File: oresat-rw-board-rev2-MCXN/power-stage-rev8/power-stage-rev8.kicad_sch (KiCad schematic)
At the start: 107 parts, among them IC1 MCXN947VDFT, J1 SM14B-SHLS-TF, J2 MEZZ, J3 Motor, U1 TCAN330, U2 MA732, U3 TPSM82901, U4 TPSM828214, U5 ADP7156ACPZ, U6 REF3030E, Y1 24 MHz

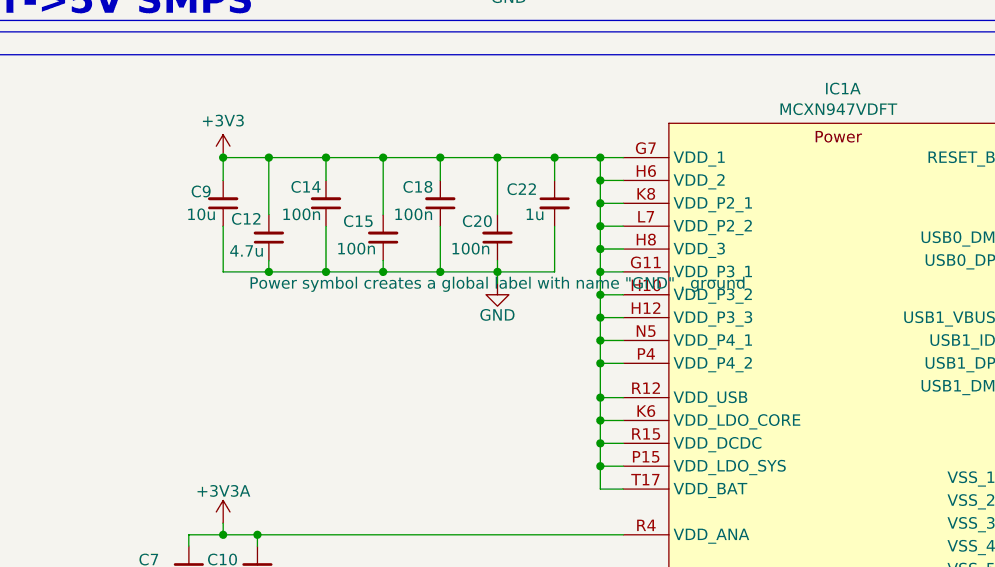
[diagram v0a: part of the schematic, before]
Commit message: mcxn V2 boards good for fab (aside from invincible silkscreen glitch???)
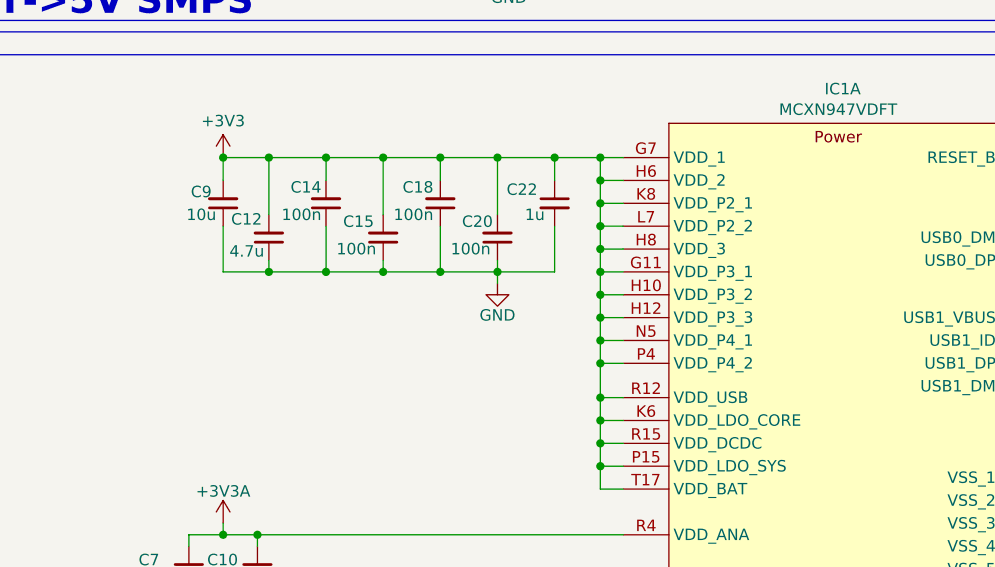
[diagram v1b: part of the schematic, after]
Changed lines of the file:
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@@
 	)
 	(symbol
-		(lib_id "rev-7-symbols:PGND")
+		(lib_id "rev-8-symbols:PGND")
 		(at 472.44 77.47 0)
 		(unit 1)
@@
 			)
 		)
-		(property "Description" ""
+		(property "Description" "Power symbol creates a global label with name \"GND\" , ground"
 			(at 472.44 77.47 0)
 			(effects
@@
 					(size 1.27 1.27)
 				)
+				(hide yes)
 			)
 		)
@@
 	)
 	(symbol
-		(lib_id "rev-7-symbols:PGND")
+		(lib_id "rev-8-symbols:PGND")
 		(at 31.75 54.61 0)
 		(unit 1)
@@
 			)
 		)
-		(property "Description" ""
+		(property "Description" "Power symbol creates a global label with name \"GND\" , ground"
 			(at 31.75 54.61 0)
 			(effects
@@
 	)
 	(symbol
-		(lib_id "rev-7-symbols:PGND")
+		(lib_id "rev-8-symbols:PGND")
 		(at 441.96 208.28 0)
 		(unit 1)
@@
 			)
 		)
-		(property "Description" ""
+		(property "Description" "Power symbol creates a global label with name \"GND\" , ground"
 			(at 441.96 208.28 0)
 			(effects
@@
 	)
 	(symbol
-		(lib_id "MCXN-rev-3-symbols:+3V3A")
+		(lib_id "rev-8-symbols:+3V3A")
 		(at 114.3 115.57 0)
 		(unit 1)
@@
 	)
 	(symbol
-		(lib_id "rev-7-symbols:PGND")
+		(lib_id "rev-8-symbols:PGND")
 		(at 57.15 54.61 0)
 		(unit 1)
@@
 			)
 		)
-		(property "Description" ""
+		(property "Description" "Power symbol creates a global label with name \"GND\" , ground"
 			(at 57.15 54.61 0)
 			(effects
@@
 	)
 	(symbol
-		(lib_id "rev-7-symbols:PGND")
+		(lib_id "rev-8-symbols:PGND")
 		(at 472.44 97.79 0)
 		(unit 1)
@@
 			)
 		)
-		(property "Description" ""
+		(property "Description" "Power symbol creates a global label with name \"GND\" , ground"
 			(at 472.44 97.79 0)
 			(effects
@@
 	)
 	(symbol
-		(lib_id "rev-7-symbols:PGND")
+		(lib_id "rev-8-symbols:PGND")
 		(at 55.88 20.32 0)
 		(unit 1)
@@
 			)
 		)
-		(property "Description" ""
+		(property "Description" "Power symbol creates a global label with name \"GND\" , ground"
 			(at 55.88 20.32 0)
 			(effects

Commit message: Formatted for *make* to work
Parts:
- C1, C10, C14, C15, C16, C18, C2, C20, C23, C28: DPN (none) -> 490-GRT155R71E104KE01JCT-ND; DST (none) -> Digikey; Dist Digikey -> (none); Dist P/N 490-GRT155R71E104KE01JCT-ND -> (none); MFR (none) -> Murata; MPN (none) -> GRT155R71E104KE01J; Mfg Murata -> (none); Mfg P/N GRT155R71E104KE01J -> (none)
- C11: DPN (none) -> 490-4762-1-ND; DST (none) -> Digikey; Dist Digikey -> (none); Dist P/N 490-4762-1-ND -> (none); MFR (none) -> Murata; MPN (none) -> GCM155R71H103KA55D; Mfg Murata -> (none); Mfg P/N GCM155R71H103KA55D -> (none)
- C12, C17, C24, C25, C27, C31, C36, C39, C40, C41, C48, C55, C7: DPN (none) -> 490-GRT155C81A475ME13JCT-ND; DST (none) -> Digikey; Dist Digikey -> (none); Dist P/N 490-GRT155C81A475ME13JCT-ND -> (none); MFR (none) -> Murata; MPN (none) -> GRT155C81A475ME13J; Mfg Murata -> (none); Mfg P/N GRT155C81A475ME13J -> (none)
- C13, C22, C37, C38, C42: DPN (none) -> 490-12238-1-ND; DST (none) -> Digikey; Dist Digikey -> (none); Dist P/N 490-12238-1-ND -> (none); MFR (none) -> Murata; MPN (none) -> GRT155C81A105ME01D; Mfg Murata -> (none); Mfg P/N GRT155C81A105ME01D -> (none)
- C19: DPN (none) -> 445-12905-2-ND; DST (none) -> Digikey; Dist Digikey -> (none); Dist P/N 445-12905-2-ND -> (none); MFR (none) -> TDK Corporation; MPN (none) -> CGA5L1X7R1C685M160AC; Mfg TDK Corporation -> (none); Mfg P/N CGA5L1X7R1C685M160AC -> (none)
- C21, C26, C29, C34, C35, C5, C9: DPN (none) -> 490-12286-1-ND; DST (none) -> Digikey; Dist Digikey -> (none); Dist P/N 490-12286-1-ND -> (none); MFR (none) -> Murata; MPN (none) -> GRT188C81C106ME13D; Mfg Murata -> (none); Mfg P/N GRT188C81C106ME13D -> (none)
- C3, C4, C49, C50, C51, C52, C53, C54, C56, C57: DPN (none) -> 490-12494-1-ND; DST (none) -> Digikey; Dist Digikey -> (none); Dist P/N 490-12494-1-ND -> (none); MFR (none) -> Murata; MPN (none) -> GRT32EC81C476KE13L; Mfg Murata -> (none); Mfg P/N GRT32EC81C476KE13L -> (none)
- C30, C43, C44: DPN (none) -> 490-GRT188C80J226ME13DCT-ND; DST (none) -> Digikey; Dist Digikey -> (none); Dist P/N 490-GRT188C80J226ME13DCT-ND -> (none); MFR (none) -> Murata; MPN (none) -> GRT188C80J226ME13D; Mfg Murata -> (none); Mfg P/N GRT188C80J226ME13D -> (none)
- C32, C33: DPN (none) -> 490-GRM1885C1H4R7WA01DCT-ND; DST (none) -> Digikey; Dist Digikey -> (none); Dist P/N 490-GRM1885C1H4R7WA01DCT-ND -> (none); MFR (none) -> Murata; MPN (none) -> GRM1885C1H4R7WA01D; Mfg Murata -> (none); Mfg P/N GRM1885C1H4R7WA01D -> (none)
- C45, C46, C47: DPN (none) -> 490-4972-1-ND; DST (none) -> Digikey; Dist Digikey -> (none); Dist P/N 490-4972-1-ND -> (none); MFR (none) -> Murata; MPN (none) -> GCM2165C2A332JA16D; Mfg Murata -> (none); Mfg P/N GCM2165C2A332JA16D -> (none)
- C6, C8: DPN (none) -> 490-12242-1-ND; DST (none) -> Digikey; Dist Digikey -> (none); Dist P/N 490-12242-1-ND -> (none); MFR (none) -> Murata; MPN (none) -> GRT155C81C225ME13D; Mfg Murata -> (none); Mfg P/N GRT155C81C225ME13D -> (none)
- D1, D2: DPN (none) -> 732-12017-2-ND; DST (none) -> Digikey; Dist Digikey -> (none); Dist P/N 732-12017-2-ND -> (none); MFR (none) -> Wurth; MPN (none) -> 150060VS55040; Mfg Wurth -> (none); Mfg P/N 150060VS55040 -> (none)
- FB1, FB5: DPN (none) -> 490-16655-1-ND; DST (none) -> Digikey; Dist Digikey -> (none); Dist P/N 490-16655-1-ND -> (none); MFR (none) -> Murata; MPN (none) -> BLM15PX601SZ1D; Mfg Murata -> (none); Mfg P/N BLM15PX601SZ1D -> (none)
- FB2, FB3, FB4: DPN (none) -> 490-13269-1-ND; DST (none) -> Digikey; Dist Digikey -> (none); Dist P/N 490-13269-1-ND -> (none); MFR (none) -> Murata; MPN (none) -> BLM31SN500SN1L; Mfg Murata -> (none); Mfg P/N BLM31SN500SN1L -> (none)
- FB6, R17, R18: DPN (none) -> 13-AC0402FR-070RLCT-ND; DST (none) -> Digikey; Dist Digikey -> (none); Dist P/N 13-AC0402FR-070RLCT-ND -> (none); MFR (none) -> Yageo; MPN (none) -> AC0402FR-070RL; Mfg Yageo -> (none); Mfg P/N AC0402FR-070RL -> (none)
- IC1: DPN (none) -> 568-MCXN947VDFT-ND; DST (none) -> Digikey; Dist Digikey -> (none); Dist P/N 568-MCXN947VDFT-ND -> (none); MFR (none) -> NXP; MPN (none) -> MCXN947VDFT; Mfg NXP -> (none); Mfg P/N MCXN947VDFT -> (none)
- J1: DPN (none) -> 455-SM14B-SHLS-TFCT-ND; DST (none) -> Digikey; Dist Digikey -> (none); Dist P/N 455-SM14B-SHLS-TFCT-ND -> (none); MFR (none) -> JST; MPN (none) -> SM14B-SHLS-TF; Mfg JST -> (none); Mfg P/N SM14B-SHLS-TF -> (none)
- J2: DPN (none) -> WM9218CT-ND; DST (none) -> Digikey; Dist Digikey -> (none); Dist P/N WM9218CT-ND -> (none); MFR (none) -> Molex; MPN (none) -> 0555600307; Mfg Molex -> (none); Mfg P/N 0555600307 -> (none)
- L1: DPN (none) -> 118-SRP2012TMA-1R5MTR-ND; DST (none) -> Digikey; Dist Digikey -> (none); Dist P/N 118-SRP2012TMA-1R5MTR-ND -> (none); MFR (none) -> Bourns Inc.; MPN (none) -> SRP2012TMA-1R5M; Mfg Bourns Inc. -> (none); Mfg P/N SRP2012TMA-1R5M -> (none)
- R1, R9: DPN (none) -> YAG5814TR-ND; DST (none) -> Digikey; Dist Digikey -> (none); Dist P/N YAG5814TR-ND -> (none); MFR (none) -> Yageo; MPN (none) -> SR0402FR-7T100RL; Mfg Yageo -> (none); Mfg P/N SR0402FR-7T100RL -> (none)
- R10, R11, R12, R13: DPN (none) -> YAG3483CT-ND; DST (none) -> Digikey; Dist Digikey -> (none); Dist P/N YAG3483CT-ND -> (none); MFR (none) -> Yageo; MPN (none) -> AC0402FR-073K3L; Mfg Yageo -> (none); Mfg P/N AC0402FR-073K3L -> (none)
- R14, R15, R16: DPN (none) -> YAG5860CT-ND; DST (none) -> Digikey; Dist Digikey -> (none); Dist P/N YAG5860CT-ND -> (none); MFR (none) -> Yageo; MPN (none) -> SR0805FR-7T12RL; Mfg Yageo -> (none); Mfg P/N SR0805FR-7T12RL -> (none)
- R19: DPN (none) -> 13-PE0402FRF470R1LCT-ND; DST (none) -> Digikey; Dist Digikey -> (none); Dist P/N 13-PE0402FRF470R1LCT-ND -> (none); MFR (none) -> Yageo; MPN (none) -> PE0402FRF470R1L; Mfg Yageo -> (none); Mfg P/N PE0402FRF470R1L -> (none)
- R2, R5: DPN (none) -> 13-AC0402DR-0710KLTR-ND; DST (none) -> Digikey; Dist Digikey -> (none); Dist P/N 13-AC0402DR-0710KLTR-ND -> (none); MFR (none) -> Yageo; MPN (none) -> AC0402DR-0710KL; Mfg Yageo -> (none); Mfg P/N AC0402DR-0710KL -> (none)
- R3: DPN (none) -> YAG3493CT-ND; DST (none) -> Digikey; Dist Digikey -> (none); Dist P/N YAG3493CT-ND -> (none); MFR (none) -> Yageo; MPN (none) -> AC0402FR-0749K9L; Mfg Yageo -> (none); Mfg P/N AC0402FR-0749K9L -> (none)
- R4: DPN (none) -> 13-AC0402FR-0776K8LCT-ND; DST (none) -> Digikey; Dist Digikey -> (none); Dist P/N 13-AC0402FR-0776K8LCT-ND -> (none); MFR (none) -> Yageo; MPN (none) -> AC0402FR-0776K8L; Mfg Yageo -> (none); Mfg P/N AC0402FR-0776K8L -> (none)
- R6: DPN (none) -> YAG6003CT-ND; DST (none) -> Digikey; Dist Digikey -> (none); Dist P/N YAG6003CT-ND -> (none); MFR (none) -> Yageo; MPN (none) -> PE0402FRF7W0R47L; Mfg Yageo -> (none); Mfg P/N PE0402FRF7W0R47L -> (none)
- R7: DPN (none) -> 13-RP0402BRD075K1LCT-ND; DST (none) -> Digikey; Dist Digikey -> (none); Dist P/N 13-RP0402BRD075K1LCT-ND -> (none); MFR (none) -> Yageo; MPN (none) -> RP0402BRD075K1L; Mfg Yageo -> (none); Mfg P/N RP0402BRD075K1L -> (none)
- R8: DPN (none) -> 13-RP0402BRD073K3LCT-ND; DST (none) -> Digikey; Dist Digikey -> (none); Dist P/N 13-RP0402BRD073K3LCT-ND -> (none); MFR (none) -> Yageo; MPN (none) -> RP0402BRD073K3L; Mfg Yageo -> (none); Mfg P/N RP0402BRD073K3L -> (none)
- TH1: DPN (none) -> 490-NCU15XH103F6SRCCT-ND; DST (none) -> Digikey; Dist Digikey -> (none); Dist P/N 490-NCU15XH103F6SRCCT-ND -> (none); MFR (none) -> Murata; MPN (none) -> NCU15XH103F6SRC; Mfg Murata -> (none); Mfg P/N NCU15XH103F6SRC -> (none)
- U1: DPN (none) -> 296-46215-1-ND; DST (none) -> Digikey; Dist Digikey -> (none); Dist P/N 296-46215-1-ND -> (none); MFR (none) -> TI; MPN (none) -> TCAN330DCNR; Mfg TI -> (none); Mfg P/N TCAN330DCNR -> (none)
- U2: DPN (none) -> 1589-MA732GQ-ZCT-ND; DST (none) -> Digikey; Dist Digikey -> (none); Dist P/N 1589-MA732GQ-ZCT-ND -> (none); MFR (none) -> MPS; MPN (none) -> MA732GQ-Z; Mfg MPS -> (none); Mfg P/N MA732GQ-Z -> (none)
- U3: DPN (none) -> 296-TPSM82901SISRCT-ND; DST (none) -> Digikey; Dist Digikey -> (none); Dist P/N 296-TPSM82901SISRCT-ND -> (none); MFR (none) -> TI; MPN (none) -> TPSM82901SISR; Mfg TI -> (none); Mfg P/N TPSM82901SISR -> (none)
- U4: DPN (none) -> 296-TPSM828214SILRCT-ND; DST (none) -> Digikey; Dist Digikey -> (none); Dist P/N 296-TPSM828214SILRCT-ND -> (none); MFR (none) -> TI; MPN (none) -> TPSM828214SILR; Mfg TI -> (none); Mfg P/N TPSM828214SILR -> (none)
- U5: DPN (none) -> 505-ADP7156ACPZ-3.3-R7CT-ND; DST (none) -> Digikey; Dist Digikey -> (none); Dist P/N 505-ADP7156ACPZ-3.3-R7CT-ND -> (none); MFR (none) -> AD; MPN (none) -> ADP7156ACPZ-3.3-R7; Mfg AD -> (none); Mfg P/N ADP7156ACPZ-3.3-R7 -> (none)
- U6: DPN (none) -> 296-26323-1-ND; DST (none) -> Digikey; Dist Digikey -> (none); Dist P/N 296-26323-1-ND -> (none); MFR (none) -> TI; MPN (none) -> REF3030AIDBZR; Mfg TI -> (none); Mfg P/N REF3030AIDBZR -> (none)
- Y1: DPN (none) -> 1923-830108212309CT-ND; DST (none) -> Digikey; Dist Digikey -> (none); Dist P/N 1923-830108212309CT-ND -> (none); MFR (none) -> Wurth; MPN (none) -> 830108212309; Mfg Wurth -> (none); Mfg P/N 830108212309 -> (none)

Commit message: ERC, DRC checking, last minute polish before fab
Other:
- title: MCXN Reaction Wheel Control Board -> MCXN Reaction Wheel Board
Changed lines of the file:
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@@
 	(paper "User" 511.82 273.05)
 	(title_block
-		(title "MCXN Reaction Wheel Control Board")
-		(rev "2")
+		(title "MCXN Reaction Wheel Board")
+		(date "2026-04-07")
+		(rev "2.0")
 		(company "Portland State Aerospace Society")
 		(comment 1 "Chris Kane-Pardy")
@@
 		)
 		(instances
-			(project ""
+			(project "power-stage-rev8"
 				(path "/dc35c2fc-4c63-4639-912e-b812884604c8"
 					(reference "U6")
@@
 		)
 		(instances
-			(project ""
+			(project "power-stage-rev8"
 				(path "/dc35c2fc-4c63-4639-912e-b812884604c8"
 					(reference "#PWR069")
@@
 		)
 		(instances
-			(project ""
+			(project "power-stage-rev8"
 				(path "/dc35c2fc-4c63-4639-912e-b812884604c8"
 					(reference "U3")
@@
 		)
 		(instances
-			(project ""
+			(project "power-stage-rev8"
 				(path "/dc35c2fc-4c63-4639-912e-b812884604c8"
 					(reference "IC1")
@@
 		)
 		(instances
-			(project ""
+			(project "power-stage-rev8"
 				(path "/dc35c2fc-4c63-4639-912e-b812884604c8"
 					(reference "#PWR061")
@@
 		)
 		(instances
-			(project ""
+			(project "power-stage-rev8"
 				(path "/dc35c2fc-4c63-4639-912e-b812884604c8"
 					(reference "#PWR041")
@@
 		)
 		(instances
-			(project ""
+			(project "power-stage-rev8"
 				(path "/dc35c2fc-4c63-4639-912e-b812884604c8"
 					(reference "IC1")
@@
 		)
 		(instances
-			(project ""
+			(project "power-stage-rev8"
 				(path "/dc35c2fc-4c63-4639-912e-b812884604c8"
 					(reference "IC1")
@@
 		)
 		(instances
-			(project ""
+			(project "power-stage-rev8"
 				(path "/dc35c2fc-4c63-4639-912e-b812884604c8"
 					(reference "IC1")
@@
 		)
 		(instances
-			(project ""
+			(project "power-stage-rev8"
 				(path "/dc35c2fc-4c63-4639-912e-b812884604c8"
 					(reference "U1")
@@
 		)
 		(instances
-			(project ""
+			(project "power-stage-rev8"
 				(path "/dc35c2fc-4c63-4639-912e-b812884604c8"
 					(reference "H1")
@@
 		)
 		(instances
-			(project ""
+			(project "power-stage-rev8"
 				(path "/dc35c2fc-4c63-4639-912e-b812884604c8"
 					(reference "#PWR033")
@@
 		)
 		(instances
-			(project ""
+			(project "power-stage-rev8"
 				(path "/dc35c2fc-4c63-4639-912e-b812884604c8"
 					(reference "IC1")
@@
 		)
 		(instances
-			(project ""
+			(project "power-stage-rev8"
 				(path "/dc35c2fc-4c63-4639-912e-b812884604c8"
 					(reference "J1")
@@
 		)
 		(instances
-			(project ""
+			(project "power-stage-rev8"
 				(path "/dc35c2fc-4c63-4639-912e-b812884604c8"
 					(reference "IC1")
@@
 		)
 		(instances
-			(project ""
+			(project "power-stage-rev8"
 				(path "/dc35c2fc-4c63-4639-912e-b812884604c8"
 					(reference "#PWR06")
@@
 		)
 		(instances
-			(project ""
+			(project "power-stage-rev8"
 				(path "/dc35c2fc-4c63-4639-912e-b812884604c8"
 					(reference "R3")
@@
 		)
 		(instances
-			(project ""
+			(project "power-stage-rev8"
 				(path "/dc35c2fc-4c63-4639-912e-b812884604c8"
 					(reference "C11")
@@
 		)
 		(instances
-			(project ""
+			(project "power-stage-rev8"
 				(path "/dc35c2fc-4c63-4639-912e-b812884604c8"
 					(reference "C8")
@@
 		)
 		(instances
-			(project ""
+			(project "power-stage-rev8"
 				(path "/dc35c2fc-4c63-4639-912e-b812884604c8"
 					(reference "C1")
@@
 		)
 		(instances
-			(project ""
+			(project "power-stage-rev8"
 				(path "/dc35c2fc-4c63-4639-912e-b812884604c8"
 					(reference "#PWR09")
@@
 		)
 		(instances
-			(project ""
+			(project "power-stage-rev8"
 				(path "/dc35c2fc-4c63-4639-912e-b812884604c8"
 					(reference "IC1")
@@
 		)
 		(instances
-			(project ""
+			(project "power-stage-rev8"
 				(path "/dc35c2fc-4c63-4639-912e-b812884604c8"
 					(reference "U4")

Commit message: Updated BOM part
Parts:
- U6: DPN 296-26323-1-ND -> 296-18517-1-ND; MPN REF3030AIDBZR -> REF3030AIDBZT
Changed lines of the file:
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@@
 			)
 		)
-		(property "DPN" "296-26323-1-ND"
+		(property "DPN" "296-18517-1-ND"
 			(at 464.82 36.83 0)
 			(effects
@@
 			)
 		)
-		(property "MPN" "REF3030AIDBZR"
+		(property "MPN" "REF3030AIDBZT"
 			(at 464.82 36.83 0)
 			(effects
